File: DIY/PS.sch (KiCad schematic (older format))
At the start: 6 parts, among them J1 PSX_PS2, J2 PSX_PS2, J3 DB25_Male, U1 LT1117-5

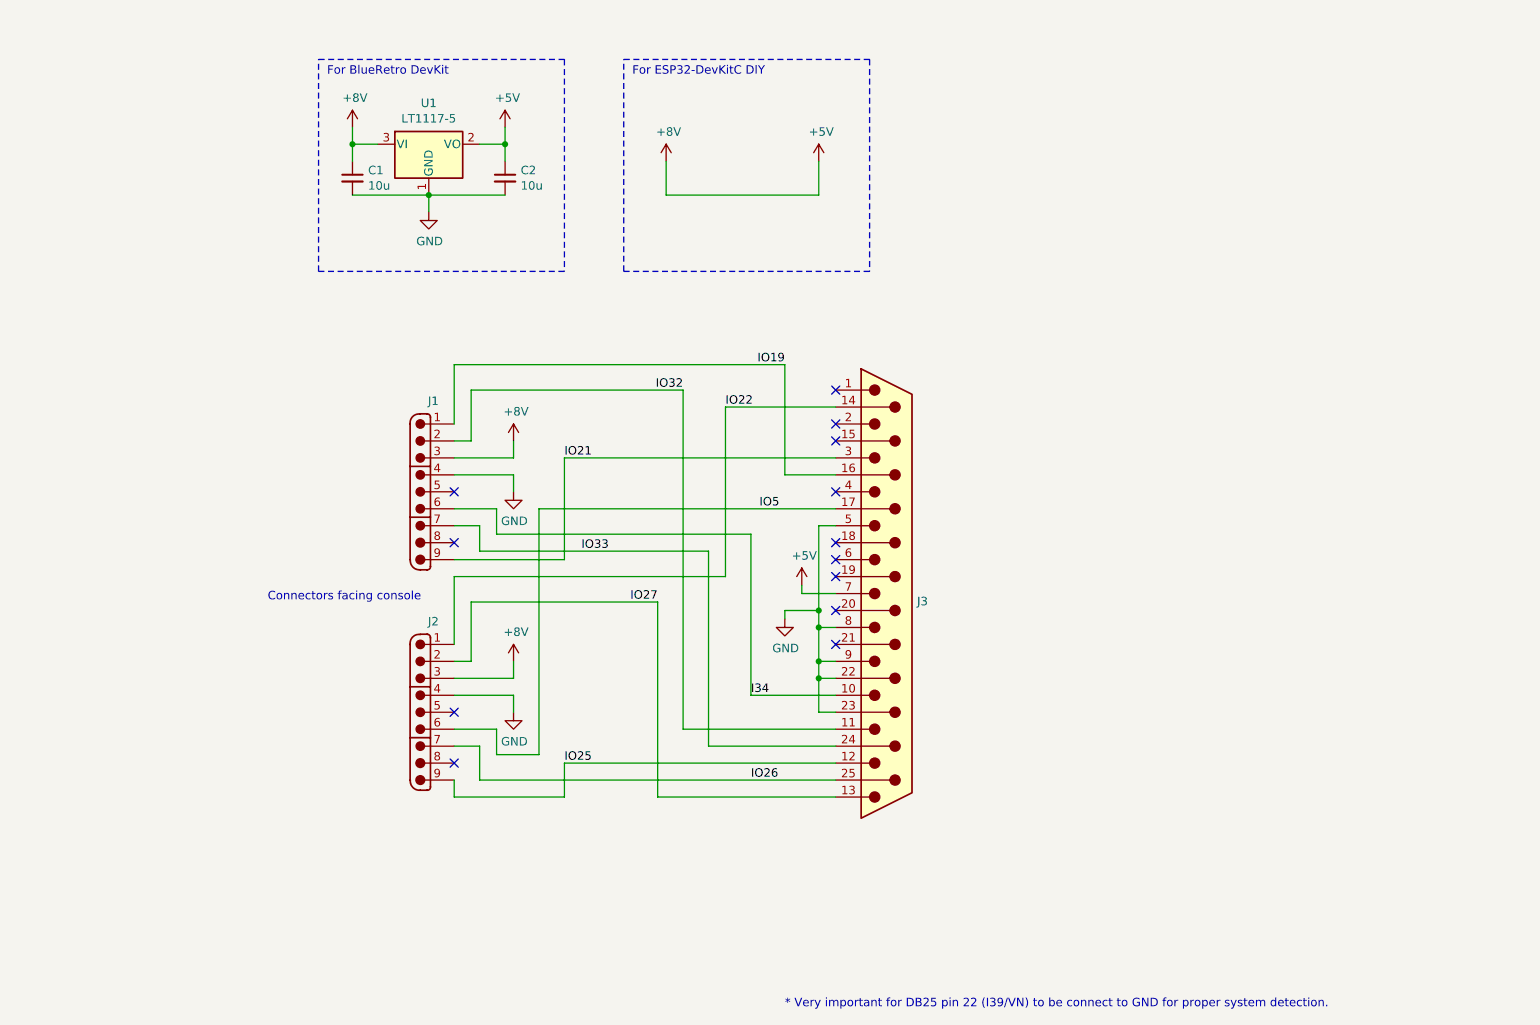
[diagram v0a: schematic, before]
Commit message: Update PS schematic base on latest info found to avoid random input
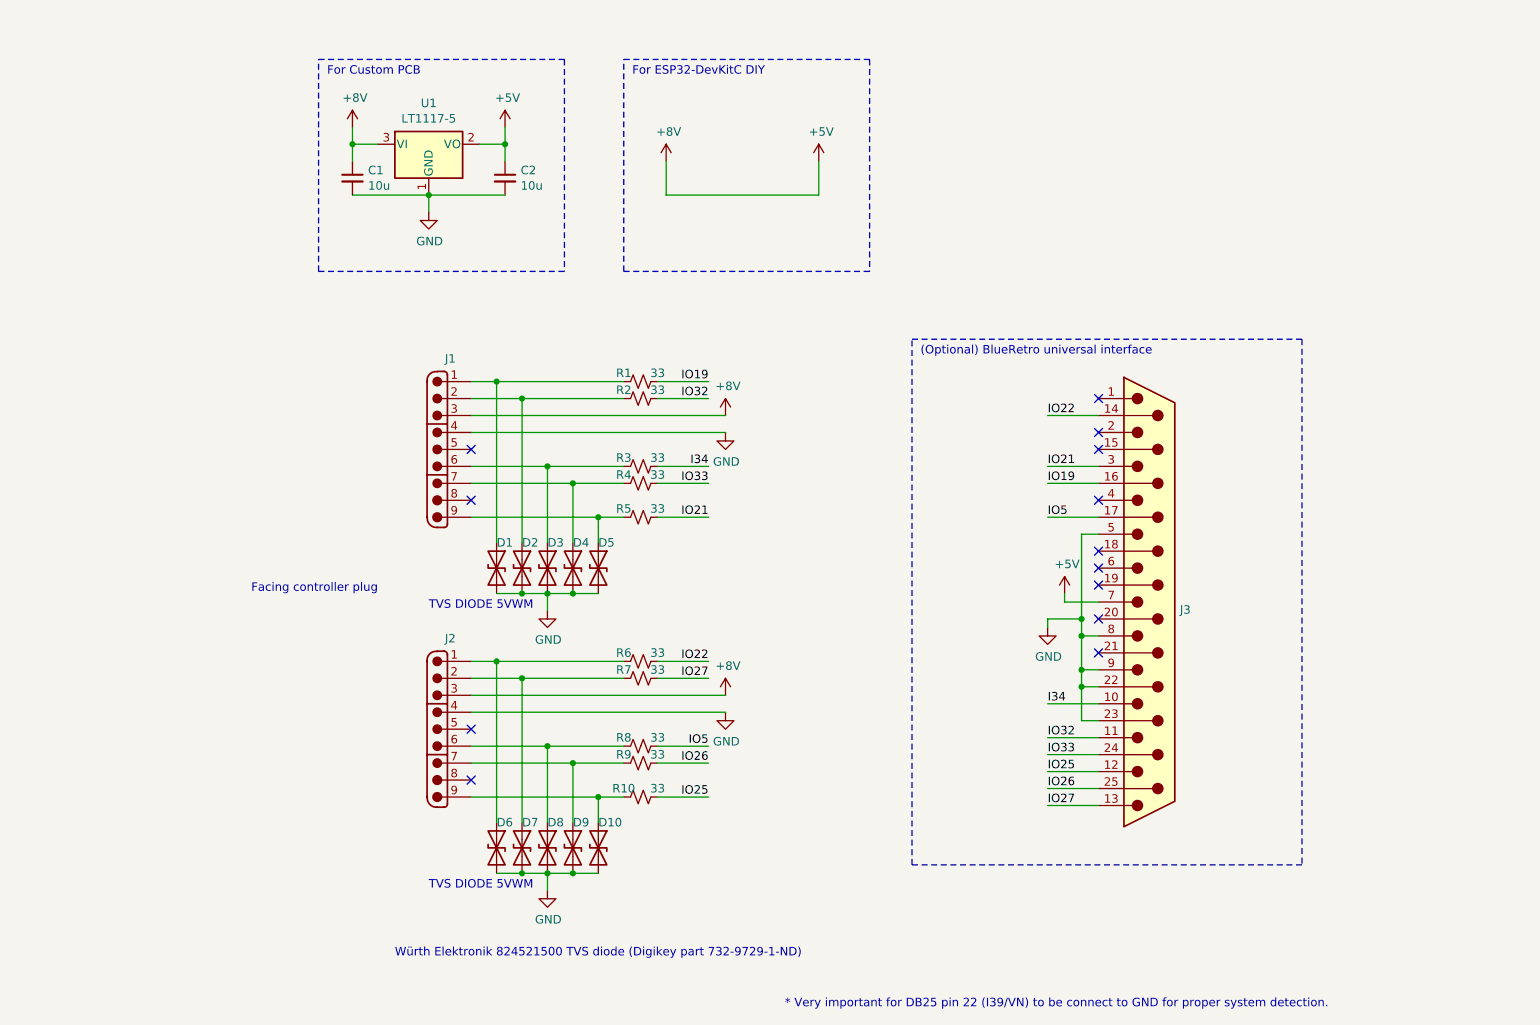
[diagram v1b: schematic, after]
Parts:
- added D1, D10, D2, D3, D4, D5, D6, D7, D8, D9: TVS DIODE 5VWM, symbol Device:D_TVS
- added R1, R10, R2, R3, R4, R5, R6, R7, R8, R9: 33, symbol Device:R_Small_US
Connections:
- net GND: now also D1.2 (A2), D10.2 (A2), D2.2 (A2), D3.2 (A2), D4.2 (A2), D5.2 (A2), D6.2 (A2), D7.2 (A2), D8.2 (A2), D9.2 (A2)
- net I34: now also R3.1; no longer J1.6
- net IO19: now also R1.1; no longer J1.1
- net IO21: now also R5.1; no longer J1.9
- net IO22: now also R6.1; no longer J2.1
- net IO25: now also R10.1; no longer J2.9
- net IO26: now also R9.1; no longer J2.7
- net IO27: now also R7.1; no longer J2.2
- net IO32: now also R2.1; no longer J1.2
- net IO33: now also R4.1; no longer J1.7
- net IO5: now also R8.1; no longer J2.6
- new net: D1.1 (A1), J1.1, R1.2
- new net: D2.1 (A1), J1.2, R2.2
- new net: D3.1 (A1), J1.6, R3.2
- new net: D4.1 (A1), J1.7, R4.2
- new net: D5.1 (A1), J1.9, R5.2
- new net: D6.1 (A1), J2.1, R6.2
- new net: D7.1 (A1), J2.2, R7.2
- new net: D8.1 (A1), J2.6, R8.2
- new net: D9.1 (A1), J2.7, R9.2
- new net: D10.1 (A1), J2.9, R10.2
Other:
- note added: "(Optional) BlueRetro universal interface"
- note added: "Facing controller plug"
- note added: "For Custom PCB"
- note added: "TVS DIODE 5VWM"
- note added: "Würth Elektronik 824521500 TVS diode (Digikey part 732-9729-1-ND)"
- note removed: "Connectors facing console"
- note removed: "For BlueRetro DevKit"
- moved on the sheet: J3

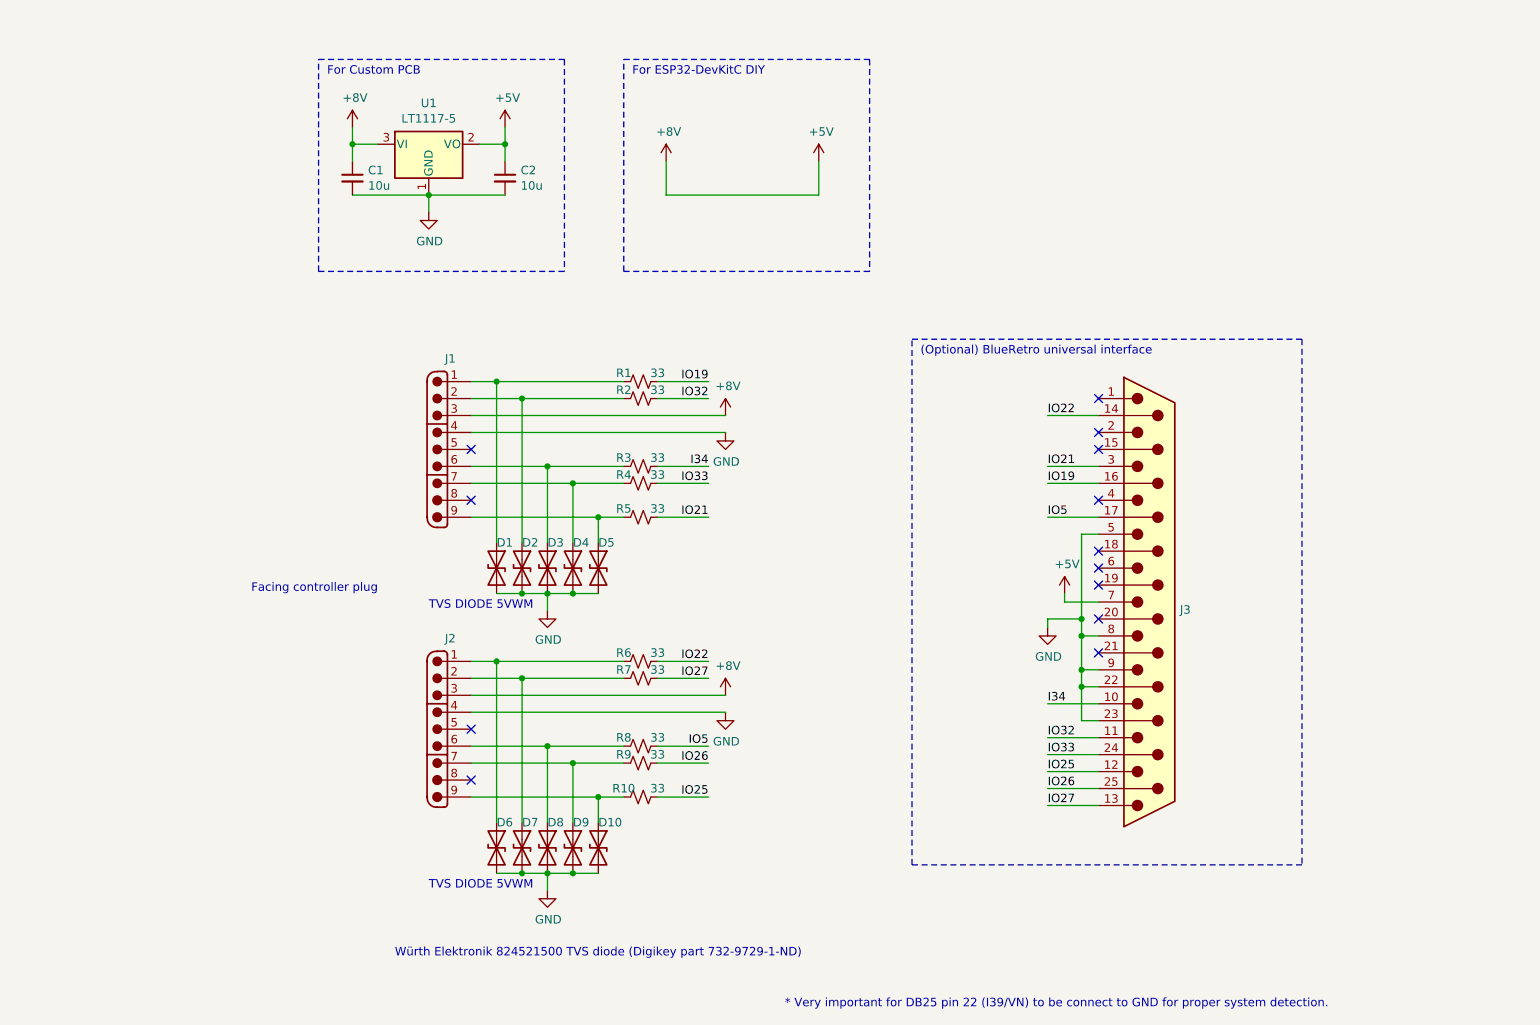
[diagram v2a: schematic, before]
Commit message: Add diode on PS power input, help with random input aswell
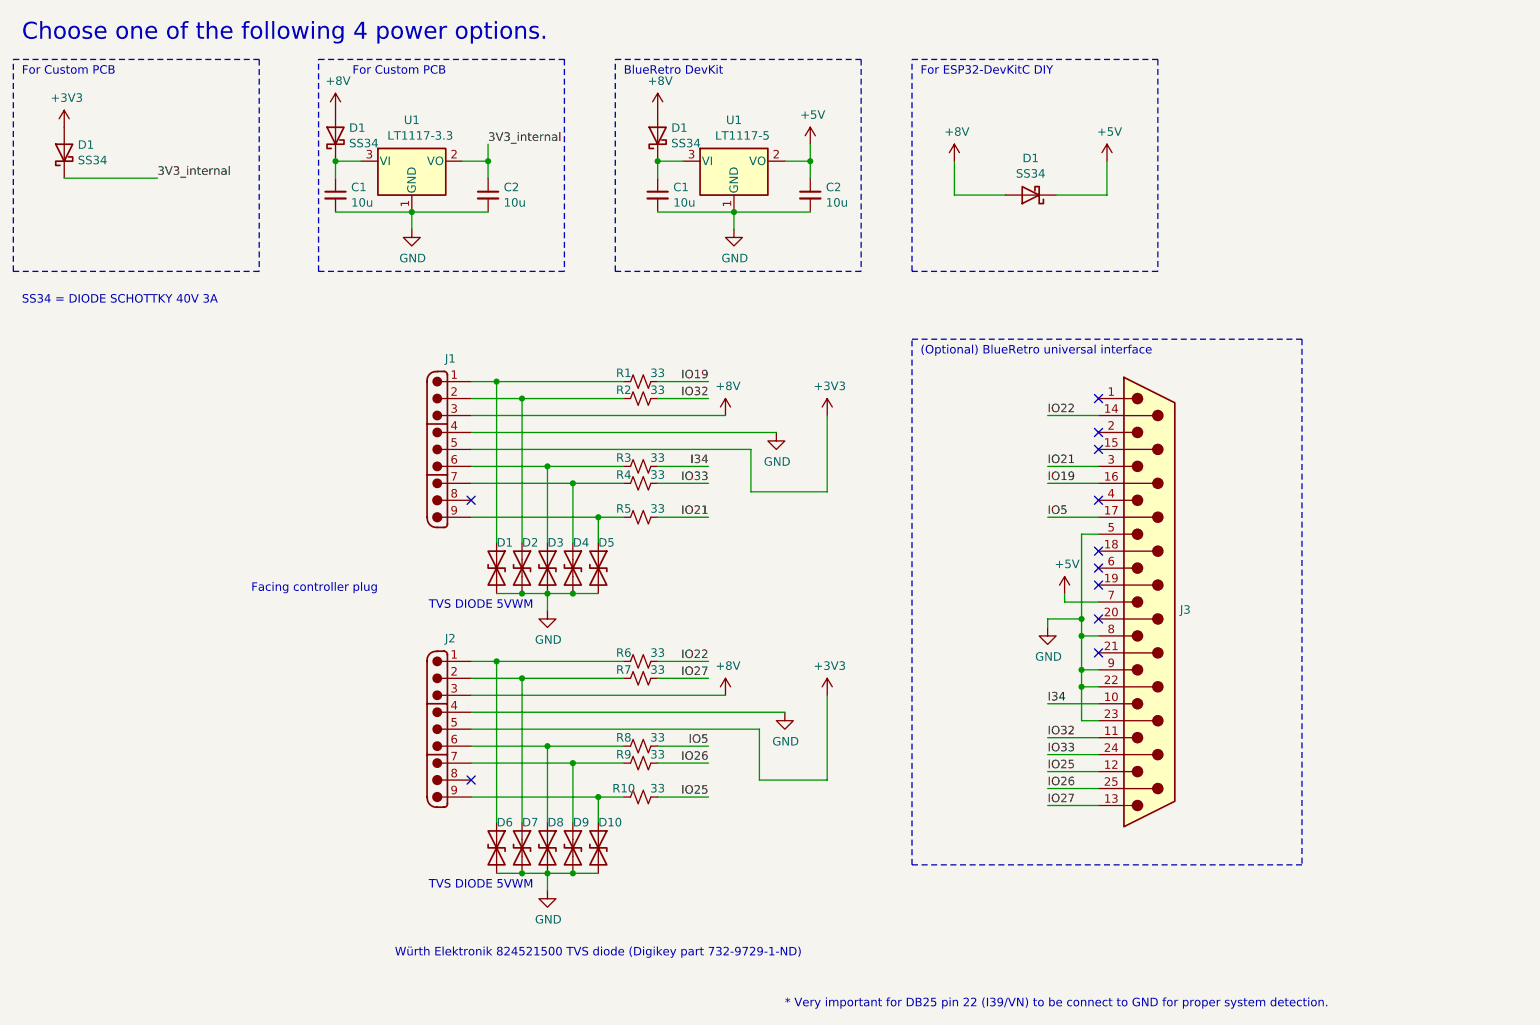
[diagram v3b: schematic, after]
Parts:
- added C1, C2: 10u, symbol Device:C_Small
- added D1 (x4): SS34, symbol Device:D_Schottky
- added U1: LT1117-5, symbol Regulator_Linear:AZ1117-5.0
- U1: value LT1117-5 -> LT1117-3.3
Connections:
- net +5V: now also C2.1, D1.1 (K), U1.2 (VO); no longer C1.1, C2.1, J1.3, J2.3, U1.2 (VO), U1.3 (VI)
- net GND: now also C1.2, C2.2, U1.1 (GND)
- net +3V3: now reaches J1.5
- net +3V3: now also J2.5, D1.2 (A)
- new net: C1.1, D1.1 (K), U1.3 (VI) (x2)
- new net +8V: D1.2 (A), D1.2 (A), D1.2 (A), J1.3, J2.3
- new net 3V3_internal: C2.1, D1.1 (K), U1.2 (VO)
- no-connect marks 13 -> 11
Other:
- note added: "BlueRetro DevKit"
- note added: "Choose one of the following 4 power options."
- note added: "SS34 = DIODE SCHOTTKY 40V 3A"
- moved on the sheet: C1, C2, U1
